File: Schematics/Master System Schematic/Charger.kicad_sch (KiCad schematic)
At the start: 14 parts, among them J10 WallSocket, J4 ChargerLV, K9 Safety Relay

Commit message: Annotations
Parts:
- renumbered F195 to F1501, F196 to F1502, F197 to F1503, F198 to F1504, F199 to F1505, F200 to F1506, HF-H12-2PIN1 to HF-H12-2PIN1501, HF-H12-2PIN2 to HF-H12-2PIN1502, J4 to J1501, J10 to J1502, K9 to K1501, PS1 to PS1501, PS2 to PS1502, R13 to R1501
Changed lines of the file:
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@@
   (symbol (lib_id "Device:Fuse") (at 137.16 67.31 90) (unit 1)
     (in_bom yes) (on_board yes)
-    (property "Reference" "F195" (id 0) (at 137.16 64.77 90))
+    (property "Reference" "F1501" (id 0) (at 137.16 64.77 90))
     (property "Value" "10A" (id 1) (at 137.16 69.85 90))
     (property "Footprint" "" (id 2) (at 137.16 69.088 90)
@@
   (symbol (lib_id "NER:TSM2500") (at 167.64 121.92 0) (mirror x) (unit 1)
     (in_bom yes) (on_board yes)
-    (property "Reference" "PS2" (id 0) (at 168.275 97.409 0))
+    (property "Reference" "PS1502" (id 0) (at 168.275 97.409 0))
     (property "Value" "TSM2500" (id 1) (at 168.275 99.7204 0))
     (property "Footprint" "" (id 2) (at 167.64 124.46 0)
@@
   (symbol (lib_id "Converter_ACDC:HLK-PM12") (at 166.37 64.77 180) (unit 1)
     (in_bom yes) (on_board yes)
-    (property "Reference" "PS1" (id 0) (at 166.37 56.7182 0))
+    (property "Reference" "PS1501" (id 0) (at 166.37 56.7182 0))
     (property "Value" "TRH100A" (id 1) (at 166.37 59.0296 0))
     (property "Footprint" "Converter_ACDC:Converter_ACDC_HiLink_HLK-PMxx" (id 2) (at 166.37 57.15 0)
@@
   (symbol (lib_id "Device:Fuse") (at 179.07 71.12 0) (unit 1)
     (in_bom yes) (on_board yes)
-    (property "Reference" "F197" (id 0) (at 172.72 71.12 0)
+    (property "Reference" "F1503" (id 0) (at 172.72 71.12 0)
       (effects (font (size 1.27 1.27)) (justify left))
     )
@@
   (symbol (lib_id "Device:Fuse") (at 203.2 114.3 90) (mirror x) (unit 1)
     (in_bom yes) (on_board yes)
-    (property "Reference" "F199" (id 0) (at 203.2 109.2962 90))
+    (property "Reference" "F1505" (id 0) (at 203.2 109.2962 90))
     (property "Value" "20A" (id 1) (at 203.2 111.6076 90))
     (property "Footprint" "" (id 2) (at 203.2 112.522 90)
@@
   (symbol (lib_id "Device:Fuse") (at 190.5 81.28 270) (unit 1)
     (in_bom yes) (on_board yes)
-    (property "Reference" "F198" (id 0) (at 190.5 76.2762 90))
+    (property "Reference" "F1504" (id 0) (at 190.5 76.2762 90))
     (property "Value" "15A" (id 1) (at 190.5 78.5876 90))
     (property "Footprint" "" (id 2) (at 190.5 79.502 90)
@@
   (symbol (lib_id "Relay:Fujitsu_FTR-F1A") (at 116.84 81.28 0) (unit 1)
     (in_bom yes) (on_board yes)
-    (property "Reference" "K9" (id 0) (at 116.84 94.4118 0))
+    (property "Reference" "K1501" (id 0) (at 116.84 94.4118 0))
     (property "Value" "Safety Relay" (id 1) (at 116.84 92.1004 0))
     (property "Footprint" "Relay_THT:Relay_DPST_Fujitsu_FTR-F1A" (id 2) (at 116.84 91.44 0)
@@
   (symbol (lib_id "Device:Fuse") (at 170.18 81.28 270) (mirror x) (unit 1)
     (in_bom yes) (on_board yes)
-    (property "Reference" "F196" (id 0) (at 170.18 78.74 90))
+    (property "Reference" "F1502" (id 0) (at 170.18 78.74 90))
     (property "Value" "15A" (id 1) (at 170.18 83.82 90))
     (property "Footprint" "" (id 2) (at 170.18 83.058 90)
@@
   (symbol (lib_id "Device:Fuse") (at 203.2 118.11 270) (mirror x) (unit 1)
     (in_bom yes) (on_board yes)
-    (property "Reference" "F200" (id 0) (at 203.2 123.1138 90))
+    (property "Reference" "F1506" (id 0) (at 203.2 123.1138 90))
     (property "Value" "20A" (id 1) (at 203.2 120.8024 90))
     (property "Footprint" "" (id 2) (at 203.2 119.888 90)
@@
   (symbol (lib_id "Connector:Conn_WallSocket_Earth") (at 199.39 86.36 0) (unit 1)
     (in_bom yes) (on_board yes)
-    (property "Reference" "J10" (id 0) (at 199.5424 98.9584 0))
+    (property "Reference" "J1502" (id 0) (at 199.5424 98.9584 0))
     (property "Value" "WallSocket" (id 1) (at 199.5424 96.647 0))
     (property "Footprint" "" (id 2) (at 191.77 83.82 0)
@@
   (symbol (lib_id "power:Earth") (at 82.55 67.31 0) (unit 1)
     (in_bom yes) (on_board yes) (fields_autoplaced)
-    (property "Reference" "#PWR02" (id 0) (at 82.55 73.66 0)
+    (property "Reference" "#PWR01501" (id 0) (at 82.55 73.66 0)
       (effects (font (size 1.27 1.27)) hide)
     )
@@
   (symbol (lib_id "NER:6_Pin_ChargerLV") (at 69.85 96.52 0) (unit 1)
     (in_bom yes) (on_board yes)
-    (property "Reference" "J4" (id 0) (at 69.85 84.709 0))
+    (property "Reference" "J1501" (id 0) (at 69.85 84.709 0))
     (property "Value" "ChargerLV" (id 1) (at 69.85 87.0204 0))
     (property "Footprint" "" (id 2) (at 67.31 96.52 0)
@@
   (symbol (lib_id "power:Earth") (at 149.86 119.38 0) (unit 1)
     (in_bom yes) (on_board yes) (fields_autoplaced)
-    (property "Reference" "#PWR03" (id 0) (at 149.86 125.73 0)
+    (property "Reference" "#PWR01503" (id 0) (at 149.86 125.73 0)
       (effects (font (size 1.27 1.27)) hide)
     )
@@
   (symbol (lib_id "Device:R") (at 88.9 102.87 0) (unit 1)
     (in_bom yes) (on_board yes)
-    (property "Reference" "R13" (id 0) (at 91.44 101.5999 0)
+    (property "Reference" "R1501" (id 0) (at 91.44 101.5999 0)
       (effects (font (size 1.27 1.27)) (justify left))
     )
@@
   (symbol (lib_id "Motor:Fan") (at 107.95 50.165 0) (unit 1)
     (in_bom yes) (on_board yes) (fields_autoplaced)
-    (property "Reference" "HF-H12-2PIN2" (id 0) (at 113.03 48.8949 0)
+    (property "Reference" "HF-H12-2PIN1502" (id 0) (at 113.03 48.8949 0)
       (effects (font (size 1.27 1.27)) (justify left))
     )
@@
   (symbol (lib_id "power:Earth") (at 82.55 105.41 0) (unit 1)
     (in_bom yes) (on_board yes) (fields_autoplaced)
-    (property "Reference" "#PWR01" (id 0) (at 82.55 111.76 0)
+    (property "Reference" "#PWR01502" (id 0) (at 82.55 111.76 0)
       (effects (font (size 1.27 1.27)) hide)
     )
@@
   (symbol (lib_id "Motor:Fan") (at 98.425 50.165 0) (mirror y) (unit 1)
     (in_bom yes) (on_board yes)
-    (property "Reference" "HF-H12-2PIN1" (id 0) (at 93.345 48.8949 0)
+    (property "Reference" "HF-H12-2PIN1501" (id 0) (at 93.345 48.8949 0)
       (effects (font (size 1.27 1.27)) (justify left))
     )
@@
   (symbol (lib_id "power:Earth") (at 185.42 92.71 0) (unit 1)
     (in_bom yes) (on_board yes) (fields_autoplaced)
-    (property "Reference" "#PWR04" (id 0) (at 185.42 99.06 0)
+    (property "Reference" "#PWR01504" (id 0) (at 185.42 99.06 0)
       (effects (font (size 1.27 1.27)) hide)
     )
@@
   (symbol (lib_id "power:Earth") (at 220.98 113.03 0) (unit 1)
     (in_bom yes) (on_board yes) (fields_autoplaced)
-    (property "Reference" "#PWR06" (id 0) (at 220.98 119.38 0)
+    (property "Reference" "#PWR01506" (id 0) (at 220.98 119.38 0)
       (effects (font (size 1.27 1.27)) hide)
     )
@@
   (symbol (lib_id "power:Earth") (at 195.58 129.54 0) (unit 1)
     (in_bom yes) (on_board yes) (fields_autoplaced)
-    (property "Reference" "#PWR05" (id 0) (at 195.58 135.89 0)
-      (effects (font (size 1.27 1.27)) hide)
-    )
+    (property "Reference" "#PWR01505" (id 0) (at 195.58 135.89 0)
+      (effects (font (size 1.27 1.27)) hide)
+    )

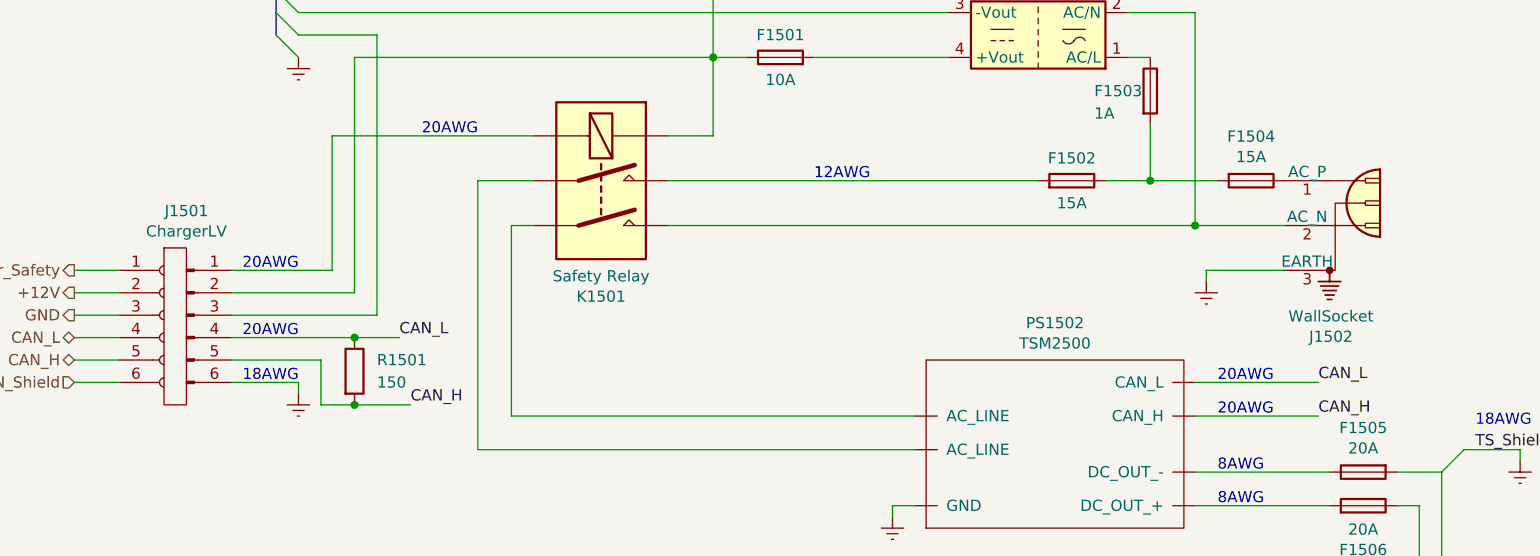
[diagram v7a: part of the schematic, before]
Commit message: Upgraded to kicad 7 and fixed dcdc
Upgraded to kicad 7
added triple-wire runs to dcdc lines
added inline fuses and glvms switch for dcdc
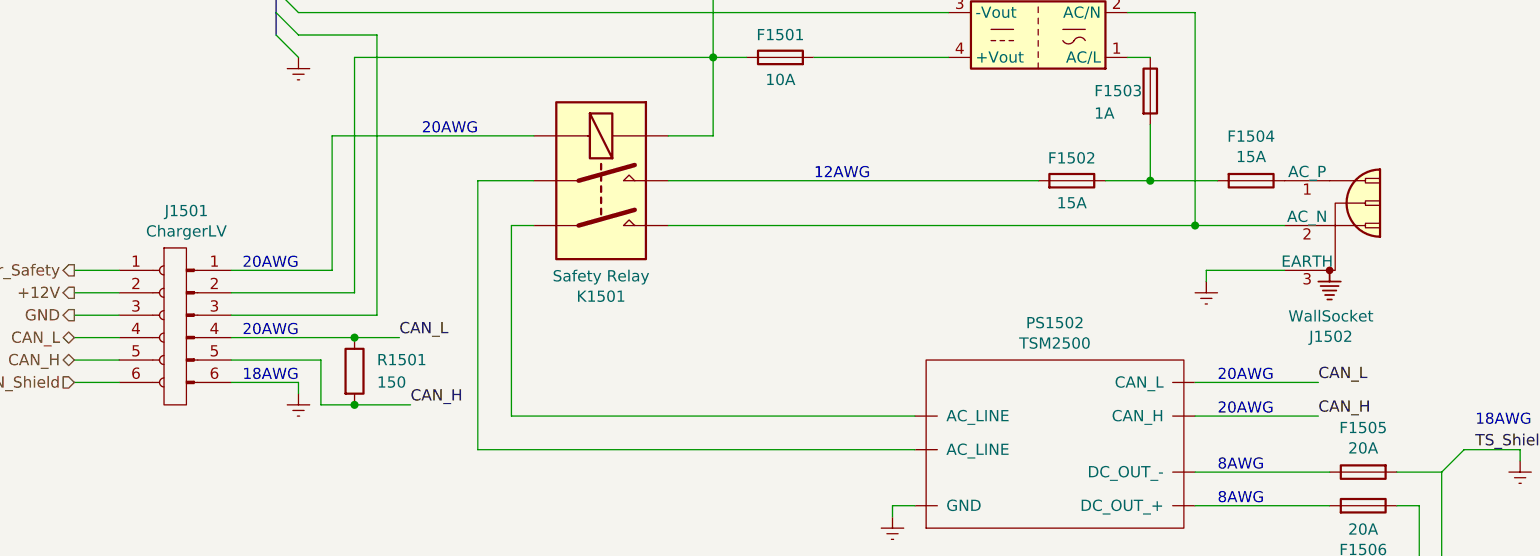
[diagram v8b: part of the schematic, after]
